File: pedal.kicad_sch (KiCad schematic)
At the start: 0 parts

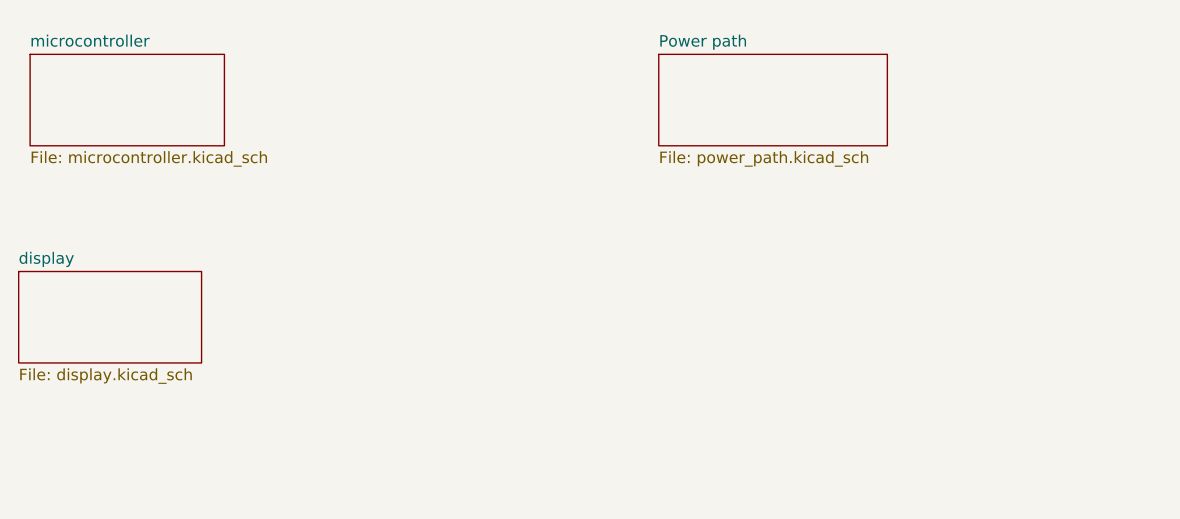
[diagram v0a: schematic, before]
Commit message: IMU (#3)
* add imu sheet and library

* routing between sheets
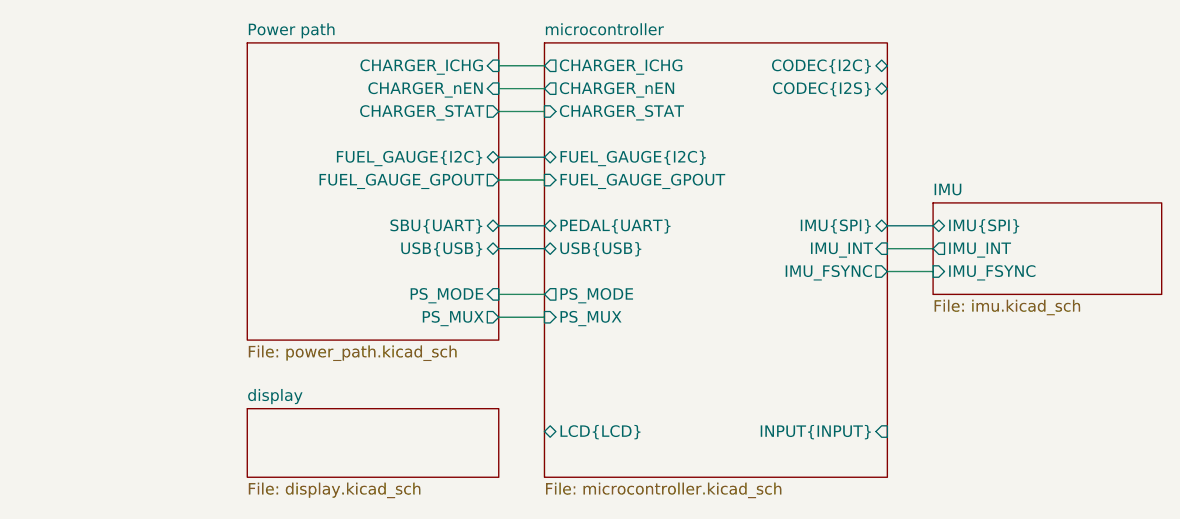
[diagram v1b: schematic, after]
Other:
- added sheet IMU (imu.kicad_sch)
- sheet Power path ports: added CHARGER_ICHG, CHARGER_STAT, CHARGER_nEN, FUEL_GAUGE_GPOUT, FUEL_GAUGE{I2C}, PS_MODE, PS_MUX, SBU{UART}, USB{USB}; removed none
- sheet microcontroller ports: added CHARGER_ICHG, CHARGER_STAT, CHARGER_nEN, CODEC{I2C}, CODEC{I2S}, FUEL_GAUGE_GPOUT, FUEL_GAUGE{I2C}, IMU_FSYNC, IMU_INT, IMU{SPI}, INPUT{INPUT}, LCD{LCD}, PEDAL{UART}, PS_MODE, PS_MUX, USB{USB}; removed none
